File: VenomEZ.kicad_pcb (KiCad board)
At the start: 2 copper layers, 72 x 42 mm, 42 parts, among them CN1 HC-XH-5A-G, CN10 HC-XH-2A-G, CN11 HC-XH-5A-G, CN2 HC-PH-8A-G, CN3 HC-XH-8A-G, CN4 HC-XH-8A-G, CN5 HC-XH-2A-G, CN6 HC-PH-7A-G, CN7 HC-XH-2A-G, CN8 HC-XH-2A-G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

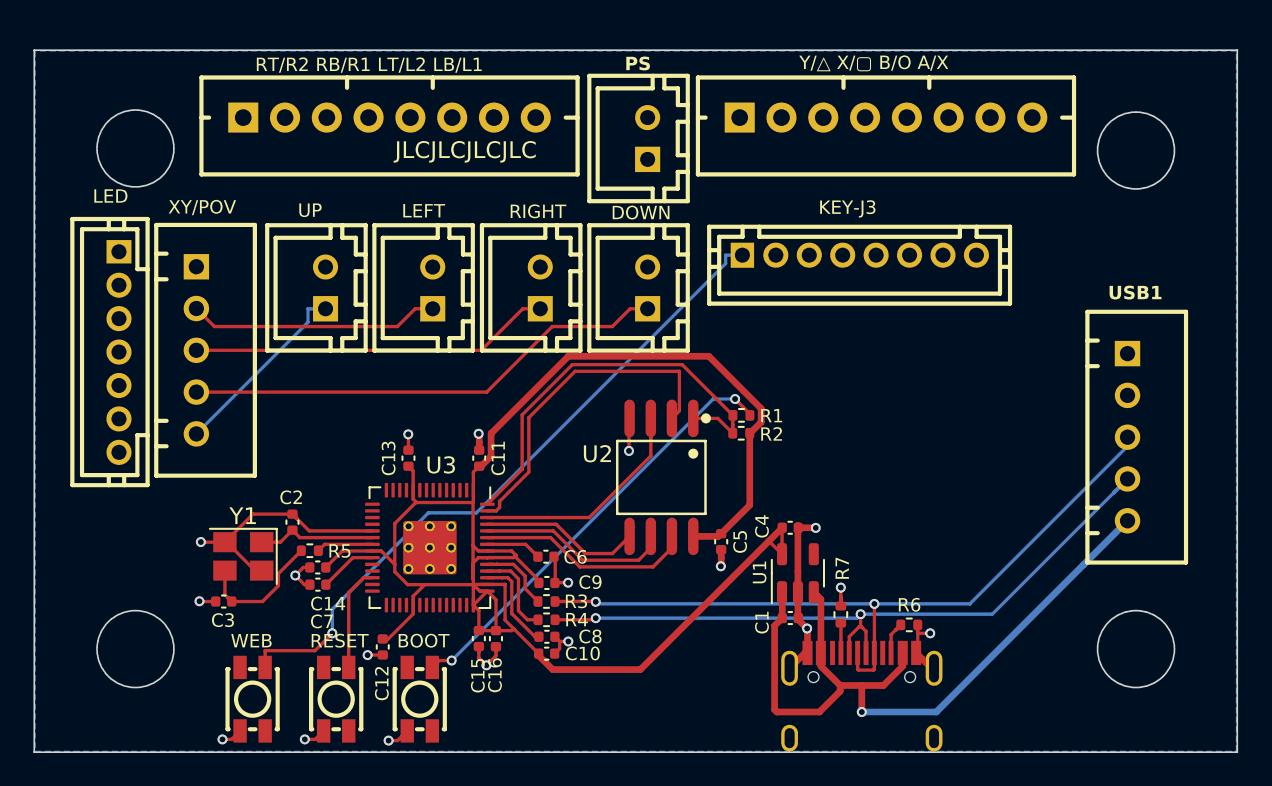
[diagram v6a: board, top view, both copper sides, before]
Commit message: Move lcsc symbols to their own library
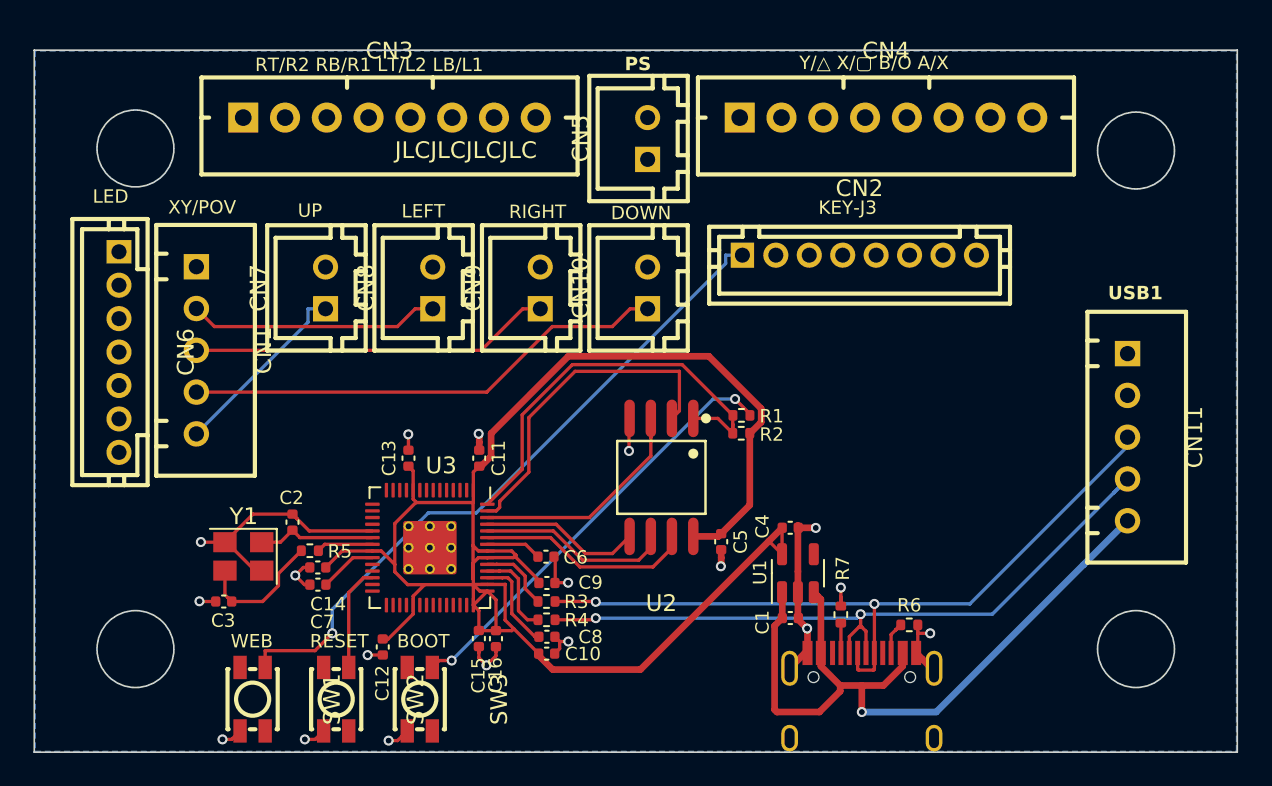
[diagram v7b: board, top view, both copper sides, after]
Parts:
- CN1, CN11: footprint easyeda2kicad:CONN-TH_5P-P2.50_HC-XH-5A-G -> lcsc:CONN-TH_5P-P2.50_HC-XH-5A-G
- CN10, CN5, CN7, CN8, CN9: footprint easyeda2kicad:CONN-TH_2P-P2.50_HC-XH-2A-G -> lcsc:CONN-TH_2P-P2.50_HC-XH-2A-G
- CN2: footprint easyeda2kicad:CONN-TH_8P-P2.00_PH-8A -> lcsc:CONN-TH_8P-P2.00_PH-8A
- CN3, CN4: footprint easyeda2kicad:CONN-TH_8P-P2.50_HCTL_XH-8A_C2908606 -> lcsc:CONN-TH_8P-P2.50_HCTL_XH-8A_C2908606
- CN6: footprint easyeda2kicad:CONN-TH_7P-P2.00_PH-7A -> lcsc:CONN-TH_7P-P2.00_PH-7A
- SW1, SW2, SW3: footprint easyeda2kicad:SW-SMD_4P-L3.6-W3.0-P1.50-LS4.7 -> lcsc:SW-SMD_4P-L3.6-W3.0-P1.50-LS4.7
- U2: footprint easyeda2kicad:SOIC-8_L5.3-W5.3-P1.27-LS8.0-BL -> lcsc:SOIC-8_L5.3-W5.3-P1.27-LS8.0-BL
